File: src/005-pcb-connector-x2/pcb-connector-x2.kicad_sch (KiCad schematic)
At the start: 11 parts

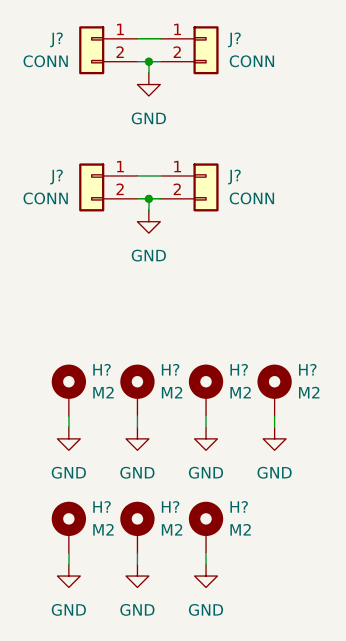
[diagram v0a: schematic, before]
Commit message: changing pcb connector x2 location
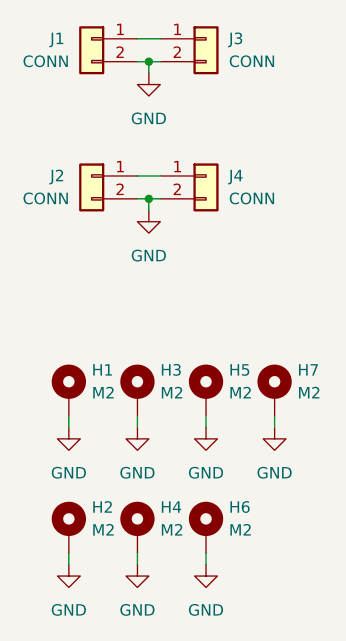
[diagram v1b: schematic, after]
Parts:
- gave numbers to parts that had none: 11

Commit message: adding filter pcb and load
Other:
- company: (none) -> Halidelabs
- title: (none) -> 005 PCB Connector x2
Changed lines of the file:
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@@
 (kicad_sch (version 20211123) (generator eeschema)
   (paper "A4")
+  (title_block
+    (title "005 PCB Connector x2")
+    (date "2022-01-28")
+    (rev "1")
+    (company "Halidelabs")
+    (comment 1 "contact@halidelabs.eu")
+  )
   (junction (at 143.51 73.66) (diameter 0) (color 0 0 0 0)
   )
